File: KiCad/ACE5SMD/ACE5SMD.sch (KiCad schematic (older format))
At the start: 90 parts, among them IC1 LM7805_TO220, IC10 74LS273, IC4 74LS04, IC5 74LS02, IC7 74LS365, IC8 74LS30, IC9 74LS365, Q1 2N3904, Q2 5MHz, Q3 BC237, U1 74LS138, X2 CRYSTALHC49U-V 6.556MHz

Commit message: Update numbering. Change footprints.
Signed-off-by: John Bradley <flypie@rocketmail.com>
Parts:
- removed unit 7 of IC4
- removed unit 5 of IC5
- removed unit 3 of Z50
- added R104, R105, R106, R107: 270, Resistor_SMD:R_0805_2012Metric, symbol Device:R
- added unit 3 of Z101
- added unit 7 of Z102
- added unit 5 of Z103
- added unit 2 of Z104
- AUDIO-IN1, AUDIO-OUT1, COMPOSITE1: footprint Connector_PinHeader_2.00mm:PinHeader_1x02_P2.00mm_Vertical -> Connector_PinSocket_2.54mm:PinSocket_1x02_P2.54mm_Vertical
- C100: renamed from C4; value 22p -> 22pf
- C101: renamed from C8; value 42p -> 42pf
- C12: footprint Capacitor_THT:CP_Radial_D5.0mm_P2.00mm -> Capacitor_SMD:CP_Elec_5x3
- C7: value 1U -> 1uf; footprint Capacitor_THT:CP_Radial_D4.0mm_P1.50mm -> Capacitor_SMD:CP_Elec_4x3.9
- C9: value 100u -> 100uf; footprint Capacitor_THT:CP_Radial_D5.0mm_P2.00mm -> Capacitor_SMD:CP_Elec_5x3
- CTC1: footprint Connector_PinHeader_2.54mm:PinHeader_2x04_P2.54mm_Vertical_SMD -> Connector_PinHeader_2.54mm:PinHeader_2x04_P2.54mm_Vertical
- IC1: footprint Package_TO_SOT_THT:TO-220-3_Vertical -> Package_TO_SOT_SMD:SOT-343_SC-70-4
- L1: footprint Inductor_THT:L_Axial_L13.0mm_D4.5mm_P5.08mm_Vertical_Fastron_HCCC -> Inductor_SMD:L_0603_1608Metric
- PIOA1, PIOB1, SIOA1, SIOB1: footprint Connector_PinHeader_2.54mm:PinHeader_2x05_P2.54mm_Vertical_SMD -> Connector_PinHeader_2.54mm:PinHeader_2x05_P2.54mm_Vertical
- Q1: value 2N3904 -> MMBT3904; footprint Package_TO_SOT_THT:TO-92_Inline -> Package_TO_SOT_SMD:SOT-23
- Q3: value BC237 -> BC847; footprint Package_TO_SOT_THT:TO-92_Inline -> Package_TO_SOT_SMD:SOT-23
- R100, R101, R102, R103: value R -> 270
- SP1: footprint Buzzer_Beeper:MagneticBuzzer_ProSignal_ABI-009-RC -> Buzzer_Beeper:PUIAudio_SMT_0825_S_4_R
- X1: renamed from X2; footprint Crystal:Crystal_HC49-U_Vertical -> Crystal:Crystal_SMD_HC49-SD
- X2: renamed from Q2; footprint Crystal:Crystal_HC49-U_Vertical -> Crystal:Crystal_SMD_HC49-SD
- Z1-2: footprint Package_SO:TSOP-I-28_11.8x8mm_P0.55mm -> Package_LCC:PLCC-32_SMD_Socket_11.4x14.0mm_P1.27mm
- Z10, Z11, Z9: value 74LS393 -> 74HCT393; footprint Package_SO:SOIC-14_3.9x8.7mm_P1.27mm -> Package_SO:TSSOP-14_4.4x5mm_P0.65mm
- Z100: renamed from U1; value 74LS138 -> 74HCT138; footprint Package_SO:SOIC-16_3.9x9.9mm_P1.27mm -> Package_SO:TSSOP-16_4.4x5mm_P0.65mm
- Z101: renamed from Z50; value 74LS21 -> 74HCT21; footprint Package_SO:SOIC-14_3.9x8.7mm_P1.27mm -> Package_SO:TSSOP-14_4.4x5mm_P0.65mm
- Z102: renamed from IC4; value 74LS04 -> 74HCT04; footprint Package_SO:SOIC-14_3.9x8.7mm_P1.27mm -> Package_SO:TSSOP-14_4.4x5mm_P0.65mm
- Z103, Z25: renamed from IC5; value 74LS02 -> 74HCT02; footprint Package_SO:SOIC-14_3.9x8.7mm_P1.27mm -> Package_SO:TSSOP-14_4.4x5mm_P0.65mm
- Z104: renamed from IC8; value 74LS30 -> 74HCT30; footprint Package_SO:SOIC-14_3.9x8.7mm_P1.27mm -> Package_SO:TSSOP-14_4.4x5mm_P0.65mm
- Z105: renamed from IC7; value 74LS365 -> 74HCT365; footprint Package_SO:SOIC-16_3.9x9.9mm_P1.27mm -> Package_SO:TSSOP-16_4.4x5mm_P0.65mm
- Z106: renamed from IC9; value 74LS365 -> 74HCT365; footprint Package_SO:SOIC-16_3.9x9.9mm_P1.27mm -> Package_SO:TSSOP-16_4.4x5mm_P0.65mm
- Z107: renamed from IC10; value 74LS273 -> 74HCT273; footprint Package_SO:SOIC-20W_7.5x12.8mm_P1.27mm -> Package_SO:TSSOP-20_4.4x6.5mm_P0.65mm
- Z12: value 74LS166 -> 74HCT166; footprint Package_SO:SOIC-16_3.9x9.9mm_P1.27mm -> Package_SO:TSSOP-16_4.4x5mm_P0.65mm
- Z13: value 74LS138 -> 74HCT138; footprint Package_SO:SOIC-16_3.9x9.9mm_P1.27mm -> Package_SO:TSSOP-16_4.4x5mm_P0.65mm
- Z14, Z15: value 74LS367 -> 74HCT367; footprint Package_SO:SOIC-16_3.9x9.9mm_P1.27mm -> Package_SO:TSSOP-16_4.4x5mm_P0.65mm
- Z19: value 74LS00 -> 74HCT00; footprint Package_SO:SOIC-14_3.9x8.7mm_P1.27mm -> Package_SO:TSSOP-14_4.4x5mm_P0.65mm
- Z20: value 74LS08 -> 74HCT08; footprint Package_SO:SOIC-14_3.9x8.7mm_P1.27mm -> Package_SO:TSSOP-14_4.4x5mm_P0.65mm
- Z21, Z22: value 74LS11 -> 74HCT11; footprint Package_SO:SOIC-14_3.9x8.7mm_P1.27mm -> Package_SO:TSSOP-14_4.4x5mm_P0.65mm
- Z23: value 74LS86 -> 74HCT86; footprint Package_SO:SOIC-14_3.9x8.7mm_P1.27mm -> Package_SO:TSSOP-14_4.4x5mm_P0.65mm
- Z24, Z25: value 74LS02 -> 74HCT02; footprint Package_SO:SOIC-14_3.9x8.7mm_P1.27mm -> Package_SO:TSSOP-14_4.4x5mm_P0.65mm
- Z27: value 74LS74 -> 74HCT74; footprint Package_SO:SOIC-14_3.9x8.7mm_P1.27mm -> Package_SO:TSSOP-14_4.4x5mm_P0.65mm
- Z3-4: footprint Package_SO:TSOP-II-32_21.0x10.2mm_P1.27mm -> Package_SO:TSOP-I-32_18.4x8mm_P0.5mm; symbol Memory_RAM:AS6C4008-55PCN -> SamacSys_Parts:AS6C4008-55TIN
- Z80CPUOUT1: footprint Connector_PinHeader_2.54mm:PinHeader_2x25_P2.54mm_Vertical_SMD -> Connector_PinHeader_2.54mm:PinHeader_2x25_P2.54mm_Vertical
- renumbered R7 to R25
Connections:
- wire segments 859 -> 868
- no-connect marks 39 -> 40

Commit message: UPdate to latest version.
Signed-off-by: John Bradley <flypie@rocketmail.com>
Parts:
- removed POWER-9V-DC1: Conn_01x02, Connector_BarrelJack:BarrelJack_CUI_PJ-036AH-SMT_Horizontal, symbol Connector_Generic:Conn_01x02
- added D100: BAT54W, Package_TO_SOT_SMD:SOT-323_SC-70, symbol Diode:BAT54W
- added HBL1, HBR1, HTL1, HTR1: MountingHole, MountingHole:MountingHole_2.5mm, symbol Mechanical:MountingHole
- added POWER-9V-DC1: PJ-036C, cuipj:CUI_PJ-036C, symbol PJ-036C:PJ-036C
- AUDIO-IN1, AUDIO-OUT1, COMPOSITE1: footprint Connector_PinSocket_2.54mm:PinSocket_1x02_P2.54mm_Vertical -> Connector_PinHeader_2.54mm:PinHeader_1x02_P2.54mm_Vertical
- IC1: footprint Package_TO_SOT_SMD:SOT-343_SC-70-4 -> Package_TO_SOT_SMD:SOT-223-3_TabPin2
- L1: value L -> 100 nH
- R1, R10, R100, R101, R102, R103, R104, R105, R106, R107, R2, R25, R3, R4, R5, R6, R9: footprint Resistor_SMD:R_0805_2012Metric -> Resistor_SMD:R_0603_1608Metric
- Z3-4: footprint Package_SO:TSOP-I-32_18.4x8mm_P0.5mm -> Package_BGA:FBGA-48_6x8_6.0x8.0mm; symbol SamacSys_Parts:AS6C4008-55TIN -> ACE5SMD-rescue:AS6C4008-55-TFBGA-SamacSys_Parts
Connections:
- wire segments 868 -> 867
- no-connect marks 40 -> 44

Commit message: Update and realign schematics. Change mount of some components.
Signed-off-by: John Bradley <flypie@rocketmail.com>
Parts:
- C11: value 100nf -> 100uf; footprint Capacitor_SMD:C_0201_0603Metric -> Capacitor_SMD:CP_Elec_3x5.3; symbol SamacSys_Parts:K104K10X7RF53H5 -> Device:CP
- Z1-2: symbol Memory_EPROM:27256 -> Memory_EPROM:27C512PLCC
- Z3-4: footprint Package_BGA:FBGA-48_6x8_6.0x8.0mm -> Package_SO:SSOP-32_11.305x20.495mm_P1.27mm; symbol ACE5SMD-rescue:AS6C4008-55-TFBGA-SamacSys_Parts -> AS6C4008:AS6C4008-SOP-DIP-TSOPII
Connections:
- wire segments 867 -> 878
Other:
- moved on the sheet: AUDIO-IN1, AUDIO-OUT1, C1, C10, C100, C101, C12, C13, C14, C15, C16, C17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

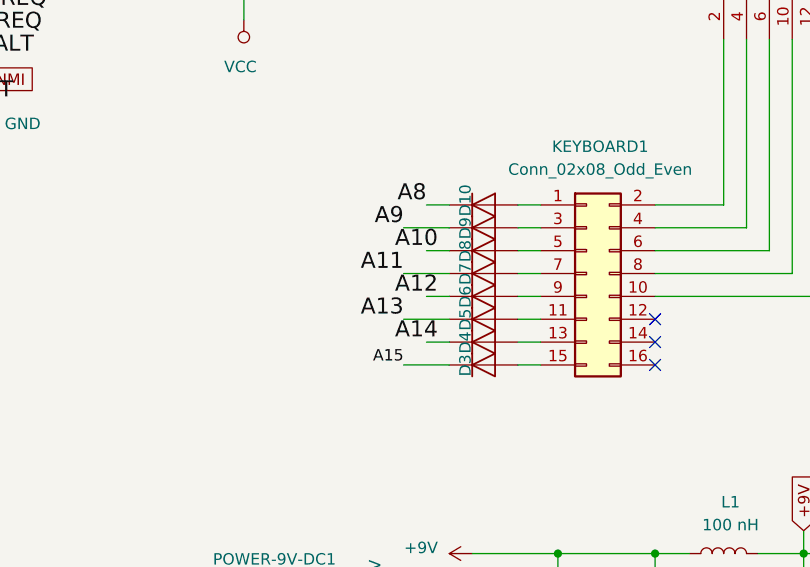
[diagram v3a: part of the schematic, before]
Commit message: Tidy add Zilog Logo.
Signed-off-by: John Bradley <flypie@rocketmail.com>
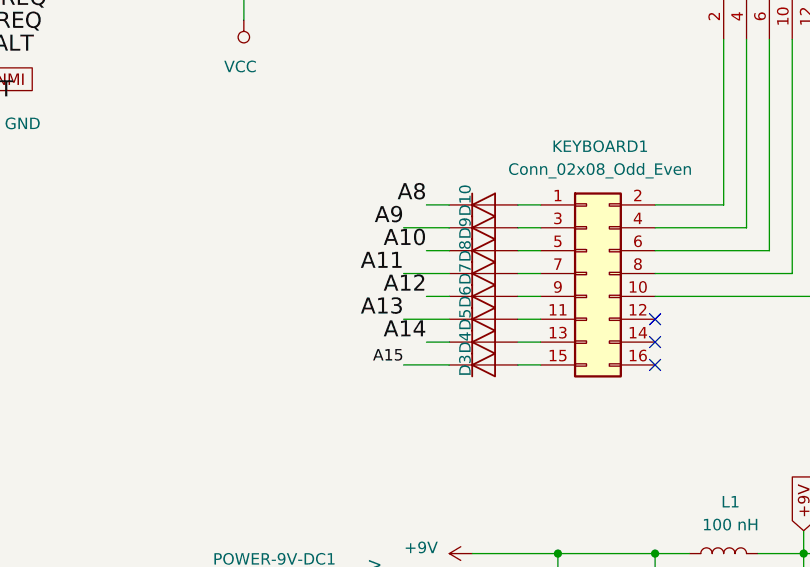
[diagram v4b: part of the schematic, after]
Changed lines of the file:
@@
 Wire Wire Line
 	7675 15500 7575 15500
-Text Label 7625 15500 2    70   ~ 0
+Text Label 7575 15500 2    70   ~ 0
 A10
 Wire Wire Line
@@
 Wire Wire Line
 	7675 15700 7575 15700
-Text Label 7625 15700 2    70   ~ 0
+Text Label 7575 15700 2    70   ~ 0
 A12
 Wire Wire Line
@@
 Wire Wire Line
 	7675 15900 7575 15900
-Text Label 7625 15900 2    70   ~ 0
+Text Label 7575 15900 2    70   ~ 0
 A14
 Wire Wire Line

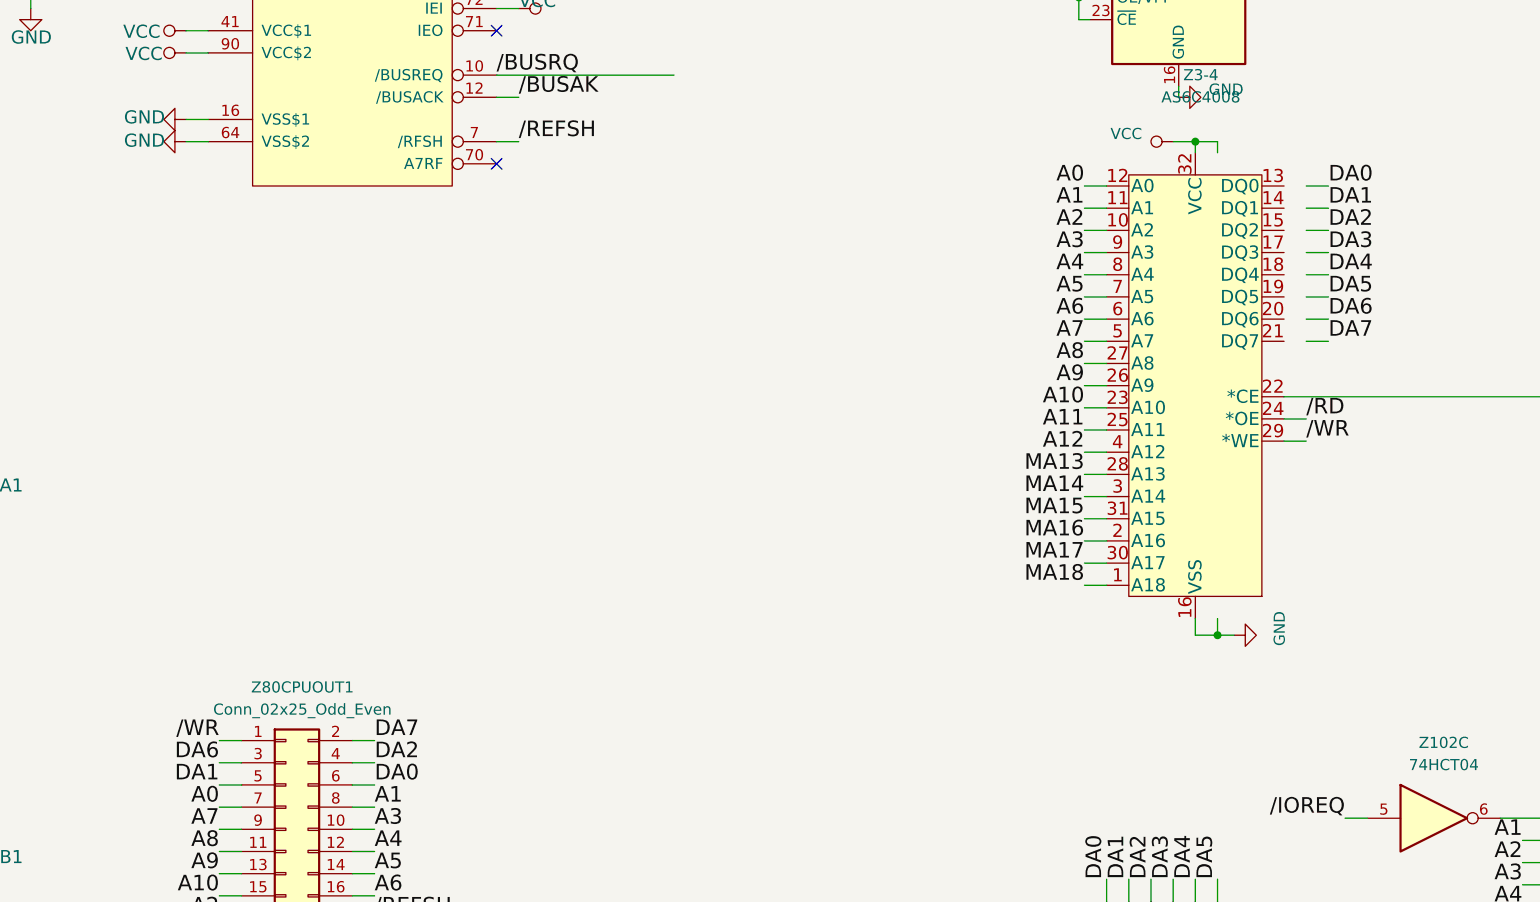
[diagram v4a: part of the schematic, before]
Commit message: Add Edge board to convert PINs to EDGECONNECTOR.
Signed-off-by: John Bradley <flypie@rocketmail.com>
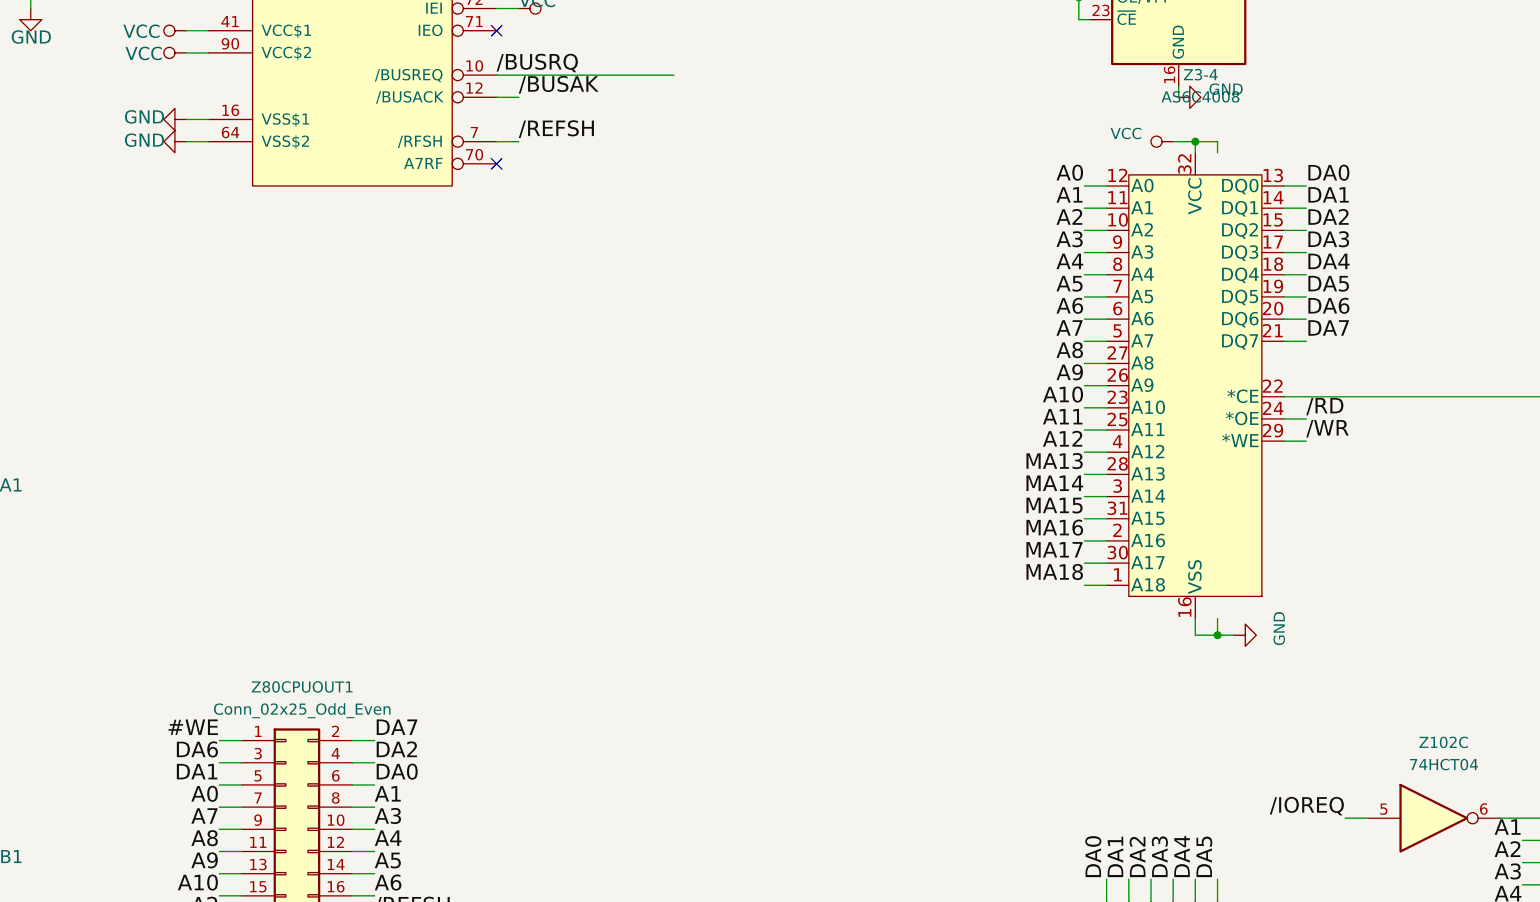
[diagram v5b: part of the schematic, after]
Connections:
- net labels added: #WE
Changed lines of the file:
@@
 	4975 12850 4875 12850
 Text Label 4875 12850 2    70   ~ 0
-/WR
+#WE
 Wire Wire Line
 	9675 11500 9775 11500
@@
 Text Label 8775 11250 2    70   ~ 0
 A9
-Text Label 9875 10650 0    70   ~ 0
+Text Label 9775 10650 0    70   ~ 0
 DA3
 Wire Wire Line
-	9775 10650 9875 10650
-Text Label 9875 10850 0    70   ~ 0
+	9675 10650 9775 10650
+Text Label 9775 10850 0    70   ~ 0
 DA5
 Wire Wire Line
-	9775 10850 9875 10850
-Text Label 9875 10350 0    70   ~ 0
+	9675 10850 9775 10850
+Text Label 9775 10350 0    70   ~ 0
 DA0
 Wire Wire Line
-	9775 10350 9875 10350
-Text Label 9875 10550 0    70   ~ 0
+	9675 10350 9775 10350
+Text Label 9775 10550 0    70   ~ 0
 DA2
 Wire Wire Line
-	9775 10550 9875 10550
-Text Label 9875 11050 0    70   ~ 0
+	9675 10550 9775 10550
+Text Label 9775 11050 0    70   ~ 0
 DA7
 Wire Wire Line
-	9775 11050 9875 11050
-Text Label 9875 10450 0    70   ~ 0
+	9675 11050 9775 11050
+Text Label 9775 10450 0    70   ~ 0
 DA1
 Wire Wire Line
-	9775 10450 9875 10450
-Text Label 9875 10750 0    70   ~ 0
+	9675 10450 9775 10450
+Text Label 9775 10750 0    70   ~ 0
 DA4
 Wire Wire Line
-	9775 10750 9875 10750
-Text Label 9875 10950 0    70   ~ 0
+	9675 10750 9775 10750
+Text Label 9775 10950 0    70   ~ 0
 DA6
 Wire Wire Line
-	9775 10950 9875 10950
+	9675 10950 9775 10950
 $Comp
 L 74xx:74LS393 Z9

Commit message: Improve consitancy.
Signed-off-by: John Bradley <flypie@rocketmail.com>
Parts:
- added R32: 1K0, Resistor_THT:R_Axial_DIN0204_L3.6mm_D1.6mm_P2.54mm_Vertical, symbol Device:R
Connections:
- wire segments 878 -> 879
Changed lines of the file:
@@
 Wire Wire Line
 	11100 7100 11100 11300
+$Comp
+L Device:R R32
+U 1 1 5E2E064A
+P 11250 7100
+F 0 "R32" V 11000 7100 50  0000 C CNN
+F 1 "1K0" V 11100 7100 50  0000 C CNN
+F 2 "Resistor_THT:R_Axial_DIN0204_L3.6mm_D1.6mm_P2.54mm_Vertical" V 11180 7100 50  0001 C CNN
+F 3 "~" H 11250 7100 50  0001 C CNN
+	1    11250 7100
+	0    1    1    0
+$EndComp
+Connection ~ 11100 7100
+Wire Wire Line
+	11400 7100 11500 7100
+Text Label 11500 7100 0    50   ~ 0
+#WE
 $EndSCHEMATC
